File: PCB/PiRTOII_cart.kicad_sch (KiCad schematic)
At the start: 15 parts, among them CN1 EDGE_CONN, CN2 MICRO_SD_SLOT, J1 CONN_SNOOP, Q1 BC547, SW1 BTN_RESET_PICO, U1 PICO, U2 74LVC245, U3 74LVC245, U4 74LVC245

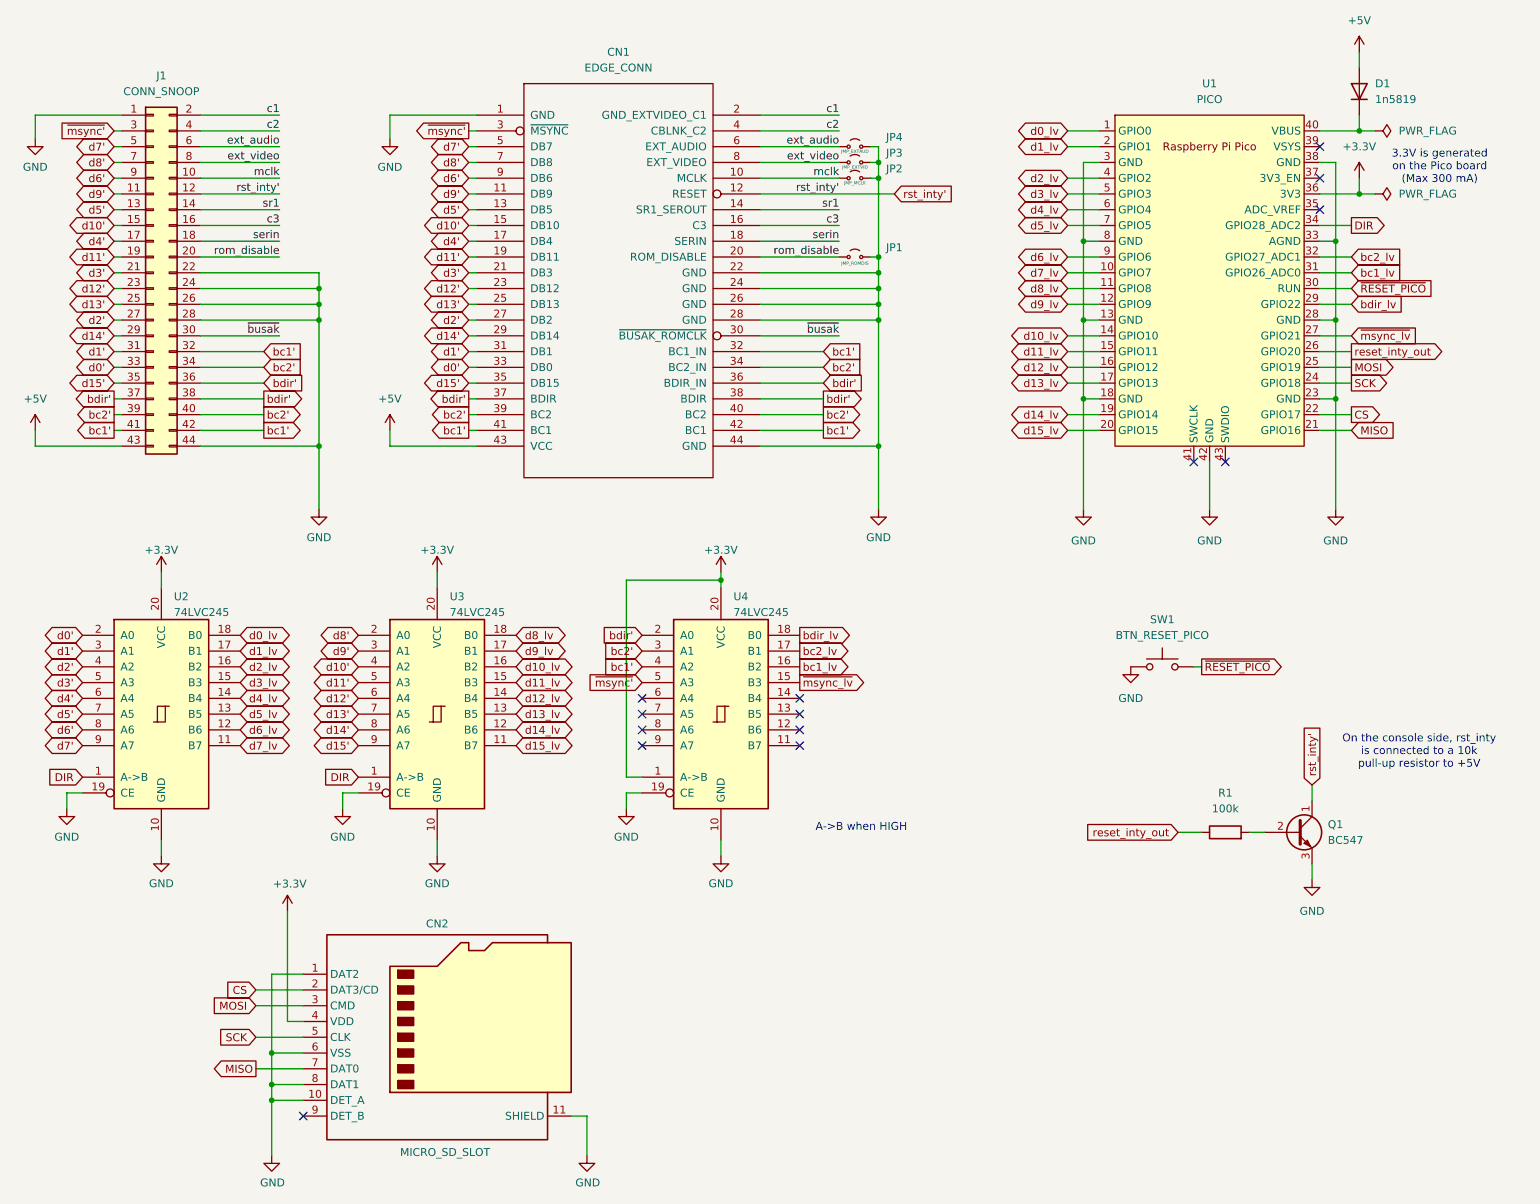
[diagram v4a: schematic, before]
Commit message: Add SD slot signal labels (?)
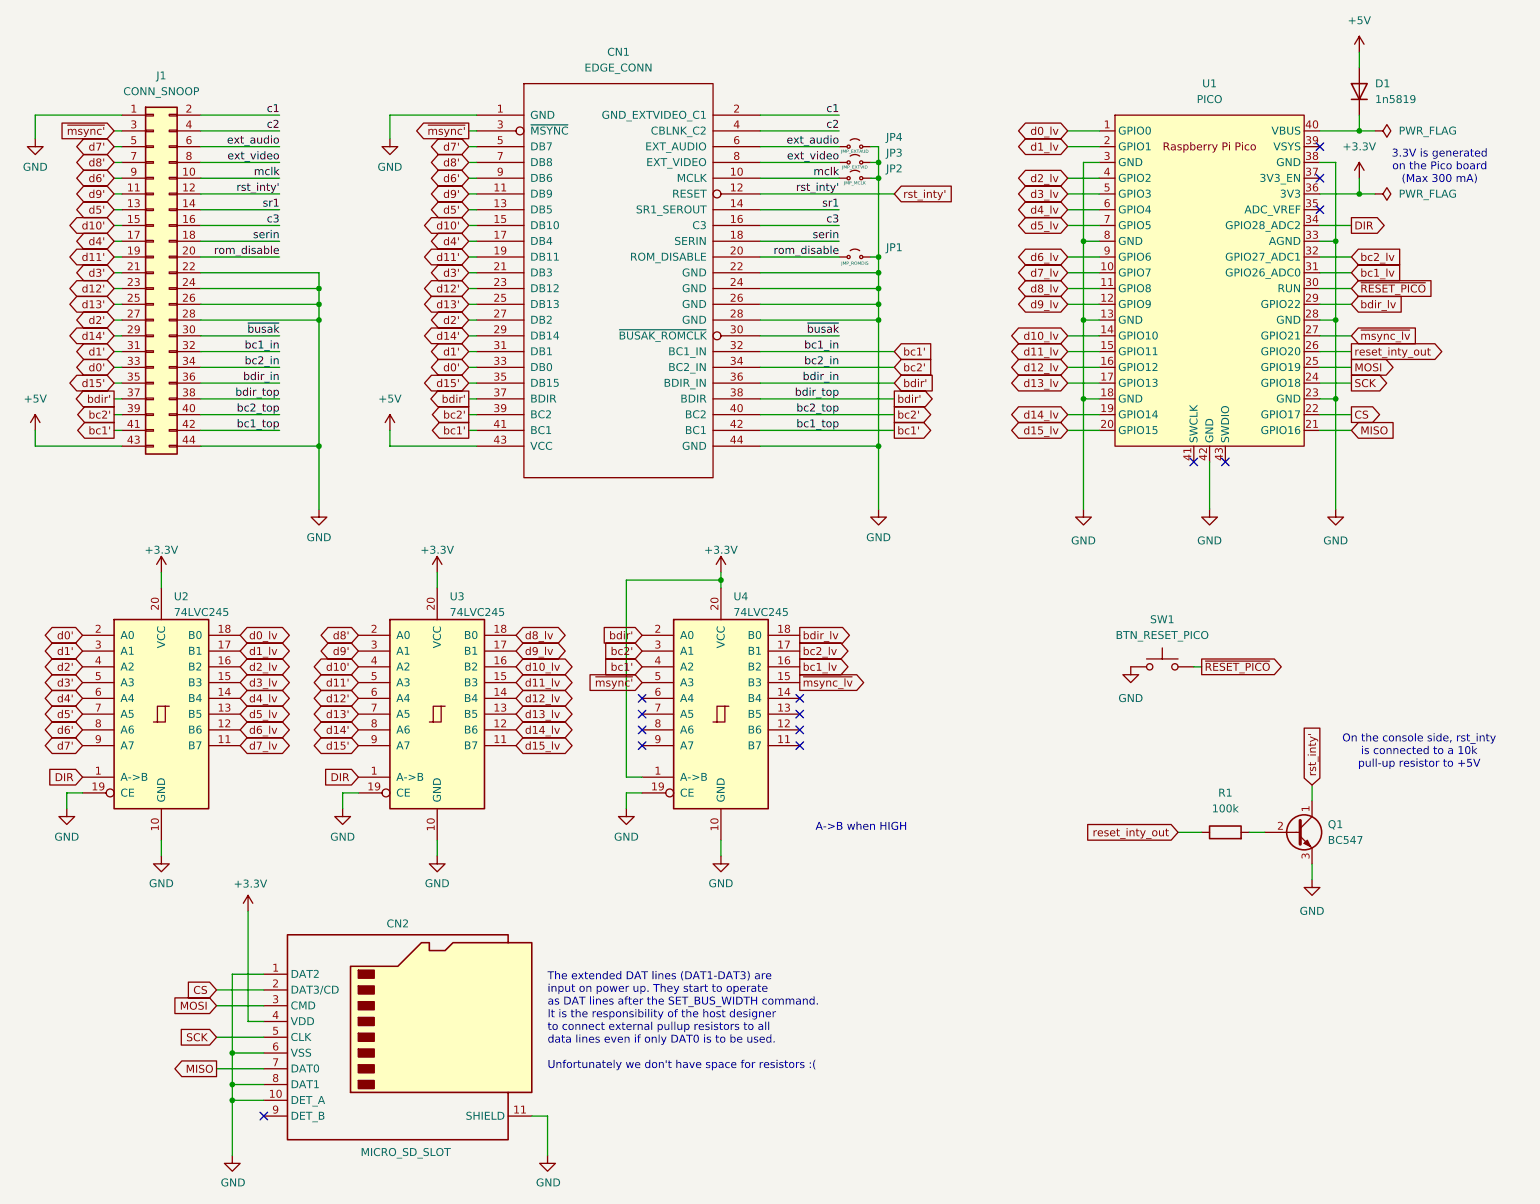
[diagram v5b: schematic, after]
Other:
- note added: "The extended DAT lines (DAT1-DAT3) are input on power up. They start to operate as DAT lines after the SET_BUS_WIDTH command. It is the responsibility of the host designer to connect external pullup resistors to all data lines even if only DAT0 is to be used. Unfortunately we don't have space for resistors :("
- moved on the sheet: CN2

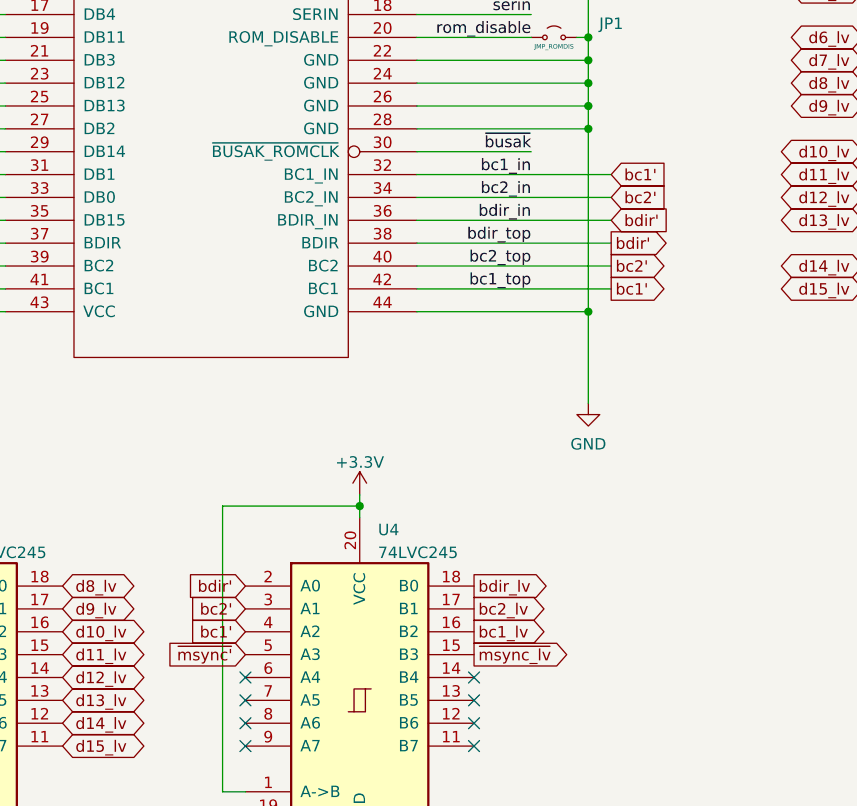
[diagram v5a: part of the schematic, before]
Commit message: Use the two BC1/2/BDIR sets more properly
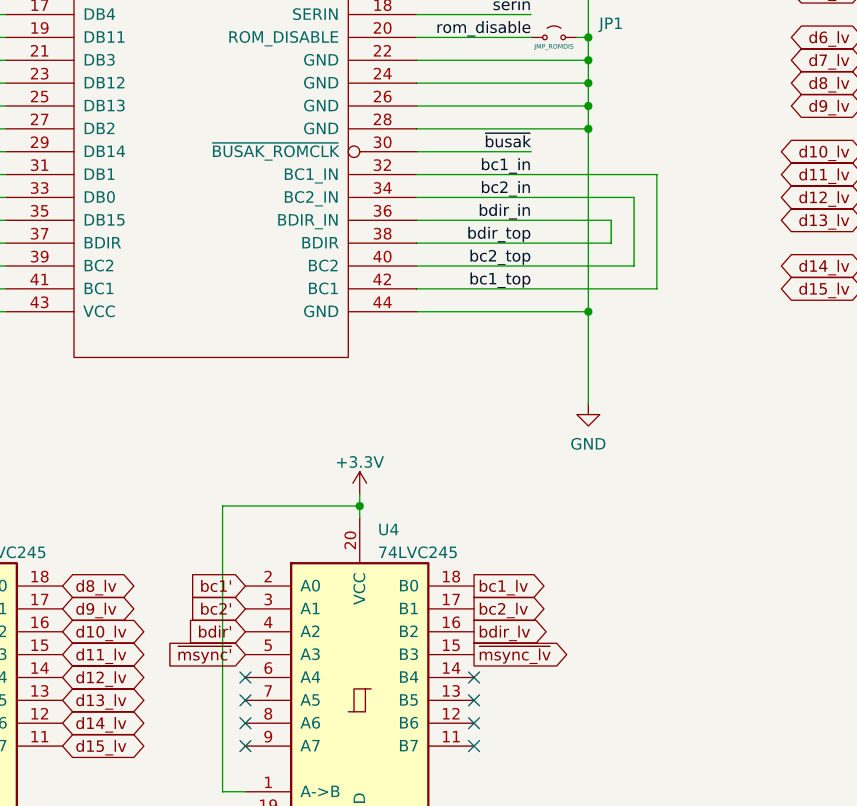
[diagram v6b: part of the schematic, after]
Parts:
- CN2: value MICRO_SD_SLOT -> MICRO_SD_SLOT
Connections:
- net bc1': now also U4.2 (A0); no longer CN1.32 (BC1_IN), CN1.42 (BC1), J1.32 (Pin_32), J1.42 (Pin_42), U4.4 (A2)
- net bc1_lv: now also U4.18 (B0); no longer U4.16 (B2)
- net bc2': no longer CN1.34 (BC2_IN), CN1.40 (BC2), J1.34 (Pin_34), J1.40 (Pin_40)
- net bdir': now also U4.4 (A2); no longer CN1.36 (BDIR_IN), CN1.38 (BDIR), J1.36 (Pin_36), J1.38 (Pin_38), U4.2 (A0)
- net bdir_lv: now also U4.16 (B2); no longer U4.18 (B0)
- new net bc1_in: CN1.32 (BC1_IN), CN1.42 (BC1), J1.32 (Pin_32), J1.42 (Pin_42)
- new net bc2_in: CN1.34 (BC2_IN), CN1.40 (BC2), J1.34 (Pin_34), J1.40 (Pin_40)
- new net bdir_in: CN1.36 (BDIR_IN), CN1.38 (BDIR), J1.36 (Pin_36), J1.38 (Pin_38)
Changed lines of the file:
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@@
 	(title_block
 		(title "PiRTO II Cart - \"Official Pico\" Edition")
-		(date "2024-07-05")
+		(date "2024-12-05")
 		(rev "2git")
 		(company "Andrea Ottaviani/SukkoPera")
@@
 	(wire
 		(pts
+			(xy 163.83 73.66) (xy 163.83 76.2)
+		)
+		(stroke
+			(width 0)
+			(type default)
+		)
+	)
+	(wire
+		(pts
 			(xy 107.95 191.77) (xy 107.95 198.12)
 		)
@@
 	(wire
 		(pts
-			(xy 142.24 68.58) (xy 163.83 68.58)
+			(xy 142.24 68.58) (xy 168.91 68.58)
 		)
 		(stroke
@@
 	(wire
 		(pts
-			(xy 142.24 78.74) (xy 163.83 78.74)
+			(xy 142.24 78.74) (xy 166.37 78.74)
 		)
 		(stroke
@@
 	(wire
 		(pts
-			(xy 142.24 81.28) (xy 163.83 81.28)
+			(xy 142.24 81.28) (xy 168.91 81.28)
 		)
 		(stroke
@@
 	(wire
 		(pts
+			(xy 168.91 68.58) (xy 168.91 81.28)
+		)
+		(stroke
+			(width 0)
+			(type default)
+		)
+	)
+	(wire
+		(pts
 			(xy 95.25 68.58) (xy 96.52 68.58)
 		)
@@
 	(wire
 		(pts
-			(xy 142.24 71.12) (xy 163.83 71.12)
+			(xy 142.24 71.12) (xy 166.37 71.12)
 		)
 		(stroke
@@
 	(wire
 		(pts
+			(xy 166.37 71.12) (xy 166.37 78.74)
+		)
+		(stroke
+			(width 0)
+			(type default)
+		)
+	)
+	(wire
+		(pts
 			(xy 95.25 73.66) (xy 96.52 73.66)
 		)
@@
 	(global_label "bdir_lv"
 		(shape output)
-		(at 148.59 114.3 0)
+		(at 148.59 119.38 0)
 		(fields_autoplaced yes)
 		(effects
@@
 		)
 		(property "Intersheetrefs" "${INTERSHEET_REFS}"
-			(at 157.8646 114.3 0)
+			(at 157.8646 119.38 0)
 			(effects
 				(font
@@
 	(global_label "bc1_lv"
 		(shape output)
-		(at 148.59 119.38 0)
+		(at 148.59 114.3 0)
 		(fields_autoplaced yes)
 		(effects
@@
 		)
 		(property "Intersheetrefs" "${INTERSHEET_REFS}"
-			(at 157.6227 119.38 0)
+			(at 157.6227 114.3 0)
 			(effects
 				(font
@@
 		)
 	)
-	(global_label "bdir'"
-		(shape input)
-		(at 163.83 73.66 0)
-		(fields_autoplaced yes)
-		(effects
-			(font
-				(size 1.27 1.27)
-			)
-			(justify left)
-		)
-		(property "Intersheetrefs" "${INTERSHEET_REFS}"
-			(at 171.109 73.66 0)
-			(effects
-				(font
-					(size 1.27 1.27)
-				)
-				(justify left)
-				(hide yes)
-			)
-		)
-	)
 	(global_label "bdir_lv"
 		(shape input)
@@
 		)
 	)
-	(global_label "bc2'"
-		(shape input)
-		(at 163.83 71.12 0)
-		(fields_autoplaced yes)
-		(effects
-			(font
-				(size 1.27 1.27)
-			)
-			(justify left)
-		)
-		(property "Intersheetrefs" "${INTERSHEET_REFS}"
-			(at 170.8671 71.12 0)
-			(effects
-				(font
-					(size 1.27 1.27)
-				)
-				(justify left)
-				(hide yes)
-			)
-		)
-	)
 	(global_label "d11'"
 		(shape bidirectional)
@@
 	(global_label "bdir'"
 		(shape input)
-		(at 123.19 114.3 180)
+		(at 123.19 119.38 180)
 		(fields_autoplaced yes)
 		(effects
@@
 		)
 		(property "Intersheetrefs" "${INTERSHEET_REFS}"
-			(at 116.4831 114.2206 0)
+			(at 116.4831 119.3006 0)
 			(effects
 				(font
@@
 		)
 	)
-	(global_label "bc2'"
-		(shape output)
-		(at 163.83 78.74 0)
-		(fields_autoplaced yes)
-		(effects
-			(font
-				(size 1.27 1.27)
-			)
-			(justify left)
-		)
-		(property "Intersheetrefs" "${INTERSHEET_REFS}"
-			(at 170.8671 78.74 0)
-			(effects
-				(font
-					(size 1.27 1.27)
-				)
-				(justify left)
-				(hide yes)
-			)
-		)
-	)
 	(global_label "d10'"
 		(shape bidirectional)
@@
 		)
 	)
-	(global_label "bc1'"
-		(shape input)
-		(at 163.83 68.58 0)
-		(fields_autoplaced yes)
-		(effects
-			(font
-				(size 1.27 1.27)
-			)
-			(justify left)
-		)
-		(property "Intersheetrefs" "${INTERSHEET_REFS}"
-			(at 170.8671 68.58 0)
-			(effects
-				(font
-					(size 1.27 1.27)
-				)
-				(justify left)
-				(hide yes)
-			)
-		)
-	)
 	(global_label "d10_lv"
 		(shape bidirectional)
@@
 		)
 	)
-	(global_label "bdir'"
-		(shape output)
-		(at 163.83 76.2 0)
-		(fields_autoplaced yes)
-		(effects
-			(font
-				(size 1.27 1.27)
-			)
-			(justify left)
-		)
-		(property "Intersheetrefs" "${INTERSHEET_REFS}"
-			(at 171.109 76.2 0)
-			(effects
-				(font
-					(size 1.27 1.27)
-				)
-				(justify left)
-				(hide yes)
-			)
-		)
-	)
 	(global_label "bc2'"
 		(shape output)
@@
 	(global_label "bc1'"
 		(shape input)
-		(at 123.19 119.38 180)
+		(at 123.19 114.3 180)
 		(fields_autoplaced yes)
 		(effects
@@
 		)
 		(property "Intersheetrefs" "${INTERSHEET_REFS}"
-			(at 116.725 119.3006 0)
+			(at 116.725 114.2206 0)
 			(effects
 				(font
@@
 		)
 	)
-	(global_label "bc1'"
-		(shape output)
-		(at 163.83 81.28 0)
-		(fields_autoplaced yes)
-		(effects
-			(font
-				(size 1.27 1.27)
-			)
-			(justify left)
-		)
-		(property "Intersheetrefs" "${INTERSHEET_REFS}"
-			(at 170.8671 81.28 0)
-			(effects
-				(font
-					(size 1.27 1.27)
-				)
-				(justify left)
-				(hide yes)
-			)
-		)
-	)
 	(global_label "bc2'"
 		(shape output)
@@
 			)
 		)
-		(property "Value" "MICRO_SD_SLOT	"
+		(property "Value" "MICRO_SD_SLOT"
 			(at 85.09 197.612 0)
 			(effects
